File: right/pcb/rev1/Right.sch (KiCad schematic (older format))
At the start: 94 parts

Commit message: added full PCB for the right side
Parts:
- C1, C2, C3, C4, C5, C6, C7: renamed from C?; footprint (none) -> Capacitor_SMD:C_0805_2012Metric
- D1, D10, D11, D12, D13, D14, D15, D16, D17, D18, D19, D2, D20, D21, D22, D23, D24, D25, D26, D27, D28, D29, D3, D30, D31, D32, D33, D34, D35, D36, D37, D38, D4, D5, D6, D7, D8, D9: renamed from D?; footprint (none) -> Diode_SMD:D_SOD-123
- MX1, MX11, MX12, MX13, MX14, MX16, MX17, MX18, MX19, MX2, MX21, MX22, MX23, MX24, MX26, MX27, MX28, MX29, MX3, MX31, MX32, MX33, MX36, MX4, MX5, MX6, MX7, MX8, MX9: renamed from MX?; footprint (none) -> MX_Only:MXOnly-1U-NoLED
- MX10, MX34: renamed from MX?; footprint (none) -> MX_Only:MXOnly-2.75U-NoLED
- MX15, MX20, MX25, MX30: renamed from MX?; footprint (none) -> MX_Only:MXOnly-1.25U-NoLED
- MX35: renamed from MX?; footprint (none) -> MX_Only:MXOnly-2U-NoLED
- MX37: renamed from MX?; footprint (none) -> MX_Only:MXOnly-2.25U-NoLED
- MX38: renamed from MX?; footprint (none) -> MX_Only:MXOnly-1.5U-NoLED
- R1, R2, R3, R4, R5, R6: renamed from R?; footprint (none) -> Resistor_SMD:R_0805_2012Metric
- SW1: renamed from SW?; footprint (none) -> random-keyboard-parts:SKQG-1155865
- U2: renamed from U?; footprint (none) -> Keebio-Parts:TRRS_Jack
- USB1: renamed from USB?; footprint (none) -> Keebio-Parts:USB-C-12-Pin-MidMount
- Y1: renamed from Y?; footprint (none) -> Crystal:Crystal_SMD_3225-4Pin_3.2x2.5mm
- gave numbers to parts that had none: 1
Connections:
- net +5V: now also USB1.11 (VBUS), USB1.2 (VBUS)
- net Split1: now also U1.27 (PD7)
- net col0: now also U1.22 (PD5)
- net col1: now also U1.25 (PD4)
- net col2: now also U1.26 (PD6); no longer MX15.1 (COL)
- net col3: now also U1.29 (PB5); no longer MX20.1 (COL)
- net col4: now also MX15.1 (COL), U1.30 (PB6); no longer MX25.1 (COL)
- net col5: now also MX20.1 (COL), U1.31 (PC6); no longer MX30.1 (COL)
- net col6: now also U1.32 (PC7); no longer MX34.1 (COL)
- net col7: now also MX30.1 (COL), MX38.1 (COL), U1.8 (PB0); no longer MX36.1 (COL)
- net col8: now also MX25.1 (COL), MX34.1 (COL), MX36.1 (COL), U1.1 (PE6); no longer MX38.1 (COL)
- net row0: now also U1.39 (PF4)
- net row1: now also U1.40 (PF1)
- net row2: now also U1.38 (PF5)
- net row3: now also U1.37 (PF6)
- net row4: now also U1.18 (PD0)

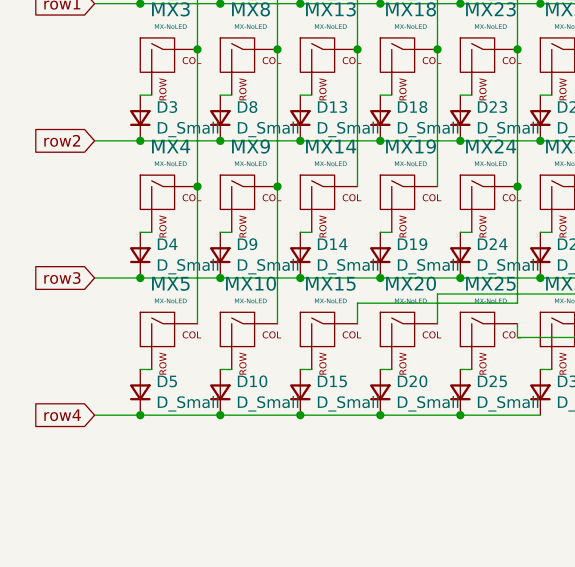
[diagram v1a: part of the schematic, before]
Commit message: Added more layouts to bottom spacebar
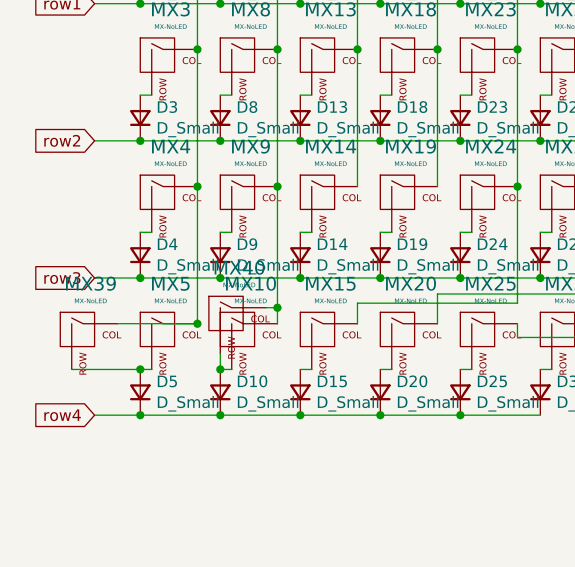
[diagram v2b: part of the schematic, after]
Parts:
- added MX39: MX-NoLED, MX_Only:MXOnly-2.75U-NoLED, symbol MX_Alps_Hybrid:MX-NoLED
- added MX40: MX-NoLED, MX_Only:MXOnly-1U-NoLED, symbol MX_Alps_Hybrid:MX-NoLED
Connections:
- net col0: now also MX39.1 (COL)
- net col1: now also MX40.1 (COL)
- net at D5.2 (A), MX5.2 (ROW): now also MX39.2 (ROW)
- net at D10.2 (A), MX10.2 (ROW): now also MX40.2 (ROW)
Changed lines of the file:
@@
 col0
 Wire Wire Line
-	1950 4310 1950 3710
+	1950 4310 1950 4240
 Connection ~ 1950 1910
 Wire Wire Line
@@
 Text GLabel 9570 3350 2    50   Input ~ 0
 col0
+$Comp
+L MX_Alps_Hybrid:MX-NoLED MX39
+U 1 1 609AA187
+P 1100 4360
+F 0 "MX39" H 1133 4583 60  0000 C CNN
+F 1 "MX-NoLED" H 1133 4509 20  0000 C CNN
+F 2 "MX_Only:MXOnly-2.75U-NoLED" H 475 4335 60  0001 C CNN
+F 3 "" H 475 4335 60  0001 C CNN
+	1    1100 4360
+	1    0    0    -1
+$EndComp
+$Comp
+L MX_Alps_Hybrid:MX-NoLED MX40
+U 1 1 609AAC87
+P 1750 4290
+F 0 "MX40" H 1783 4513 60  0000 C CNN
+F 1 "MX-NoLED" H 1783 4439 20  0000 C CNN
+F 2 "MX_Only:MXOnly-1U-NoLED" H 1125 4265 60  0001 C CNN
+F 3 "" H 1125 4265 60  0001 C CNN
+	1    1750 4290
+	1    0    0    -1
+$EndComp
+Wire Wire Line
+	1700 4440 1700 4510
+Connection ~ 1700 4510
+Wire Wire Line
+	1900 4240 1950 4240
+Connection ~ 1950 4240
+Wire Wire Line
+	1950 4240 1950 3710
+Wire Wire Line
+	1050 4510 1350 4510
+Connection ~ 1350 4510
+Wire Wire Line
+	1250 4310 1600 4310
+Connection ~ 1600 4310
 $EndSCHEMATC
